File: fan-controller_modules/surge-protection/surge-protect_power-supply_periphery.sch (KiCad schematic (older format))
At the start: 23 parts

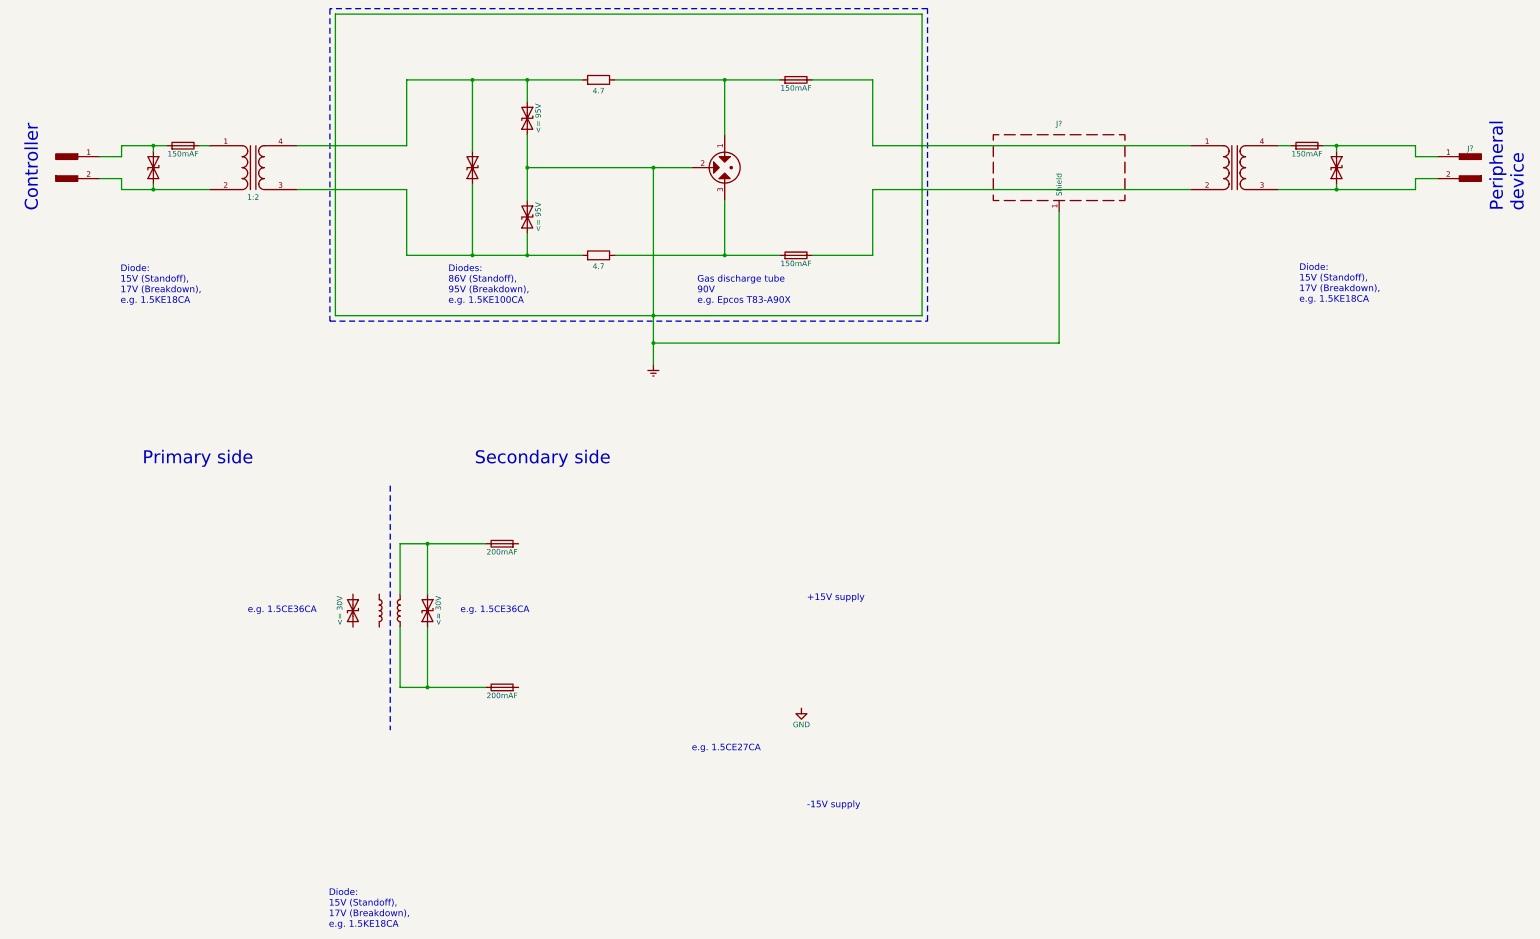
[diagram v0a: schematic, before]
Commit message: Modifying surge protection.
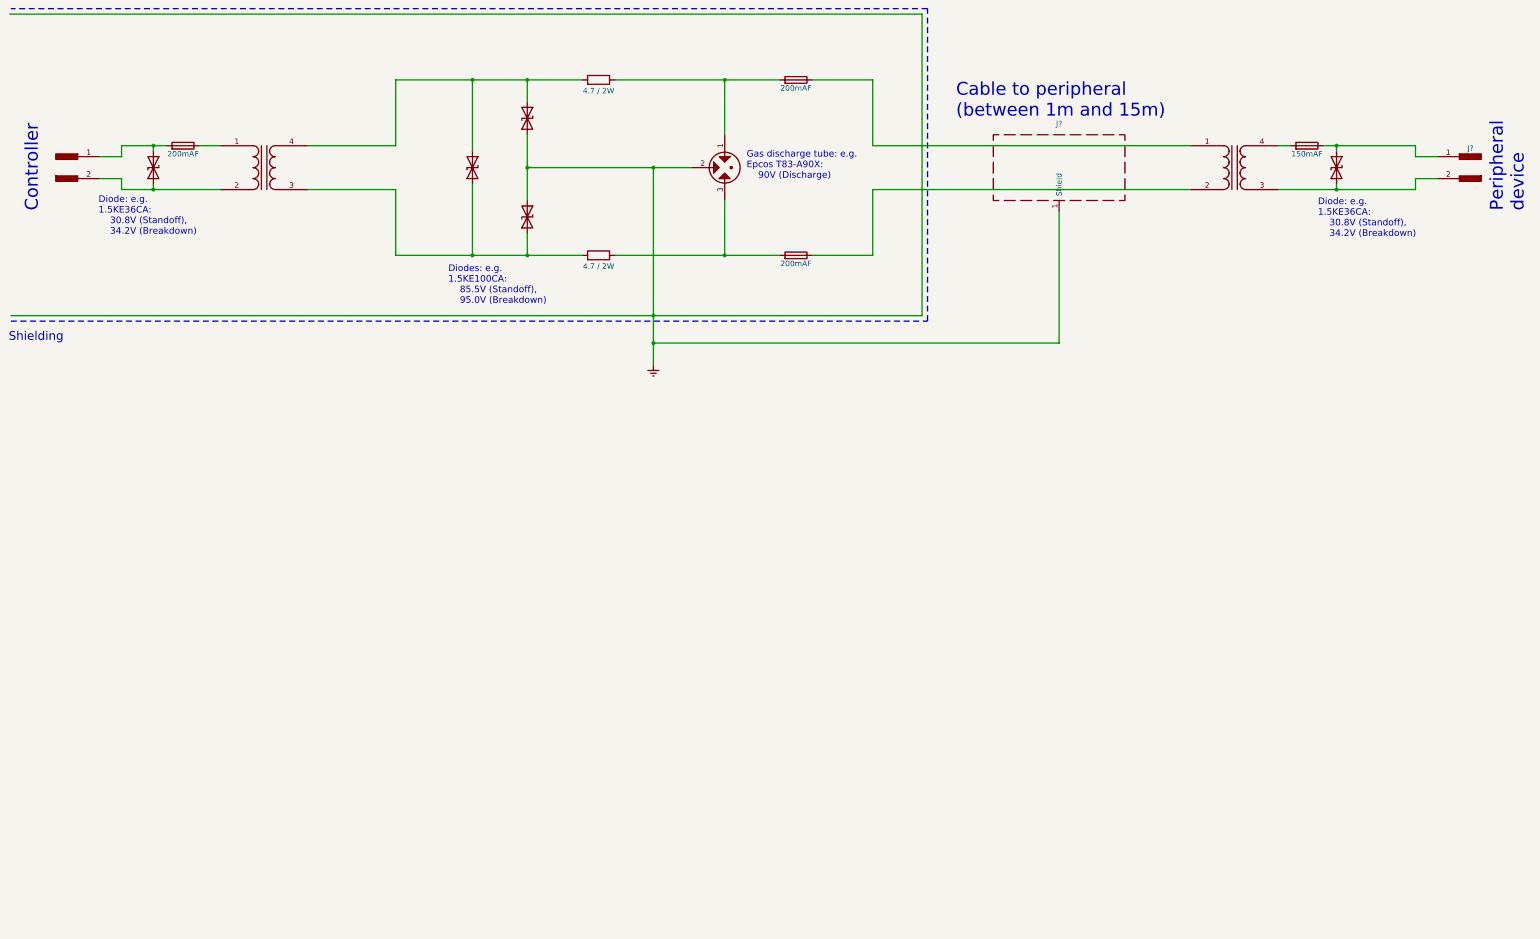
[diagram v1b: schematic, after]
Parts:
- removed D? (x2): <= 30V, symbol D_TVS
- removed F? (x2): 200mAF, symbol Fuse
- removed L? (x2): L, symbol L
- removed T?: 1:2, symbol Transformer_1P_1S
- added T?: 2:1, symbol Transformer_1P_1S
- F? (x3): value 150mAF -> 200mAF
- R? (x2): value 4.7 -> 4.7 / 2W
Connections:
- net labels removed: GND
- wire segments 53 -> 61
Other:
- note added: "Cable to peripheral\n(between 1m and 15m)"
- note added: "Diode: e.g.\n1.5KE36CA:\n 30.8V (Standoff),\n 34.2V (Breakdown)\n"
- note added: "Diodes: e.g.\n1.5KE100CA:\n 85.5V (Standoff),\n 95.0V (Breakdown)"
- note added: "Gas discharge tube: e.g.\nEpcos T83-A90X:\n 90V (Discharge)"
- note added: "Shielding"
- note removed: "+15V supply"
- note removed: "-15V supply"
- note removed: "Diode: \n15V (Standoff),\n17V (Breakdown),\ne.g. 1.5KE18CA"
- note removed: "Diodes: \n86V (Standoff),\n95V (Breakdown),\ne.g. 1.5KE100CA"
- note removed: "Gas discharge tube\n90V\ne.g. Epcos T83-A90X"
- note removed: "Primary side"
- note removed: "Secondary side"
- note removed: "e.g. 1.5CE27CA"
- note removed: "e.g. 1.5CE36CA"
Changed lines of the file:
@@
 encoding utf-8
 Sheet 4 4
-Title ""
+Title "Surge protection, periphery power"
 Date ""
 Rev ""
@@
 $Comp
 L D_TVS D?
-U 1 1 59960DDD
-P 4680 9220
-F 0 "D?" H 4680 9320 50  0001 C CNN
-F 1 "<= 30V" H 4680 9340 50  0000 C CNN
-F 2 "" H 4680 9220 50  0001 C CNN
-F 3 "" H 4680 9220 50  0001 C CNN
-	1    4680 9220
-	0    -1   1    0
-$EndComp
-$Comp
-L D_TVS D?
-U 1 1 59960DE3
-P 5360 9220
-F 0 "D?" H 5360 9320 50  0001 C CNN
-F 1 "<= 30V" H 5360 9120 50  0000 C CNN
-F 2 "" H 5360 9220 50  0001 C CNN
-F 3 "" H 5360 9220 50  0001 C CNN
-	1    5360 9220
-	0    -1   1    0
-$EndComp
-$Comp
-L Fuse F?
-U 1 1 59960DE9
-P 6040 8610
-F 0 "F?" V 6120 8610 50  0001 C CNN
-F 1 "200mAF" V 5965 8610 50  0000 C CNN
-F 2 "" V 5970 8610 50  0001 C CNN
-F 3 "" H 6040 8610 50  0001 C CNN
-	1    6040 8610
-	0    -1   -1   0
-$EndComp
-$Comp
-L Fuse F?
-U 1 1 59960DEF
-P 6040 9920
-F 0 "F?" V 6120 9920 50  0001 C CNN
-F 1 "200mAF" V 5965 9920 50  0000 C CNN
-F 2 "" V 5970 9920 50  0001 C CNN
-F 3 "" H 6040 9920 50  0001 C CNN
-	1    6040 9920
-	0    -1   -1   0
-$EndComp
-$Comp
-L GND #PWR?
-U 1 1 59960DF5
-P 8770 10110
-F 0 "#PWR?" H 8770 9860 50  0001 C CNN
-F 1 "GND" H 8770 9960 50  0000 C CNN
-F 2 "" H 8770 10110 50  0001 C CNN
-F 3 "" H 8770 10110 50  0001 C CNN
-	1    8770 10110
-	1    0    0    -1
-$EndComp
-Text Notes 3720 9250 0    59   ~ 0
-e.g. 1.5CE36CA
-Text Notes 7770 10510 0    59   ~ 0
-e.g. 1.5CE27CA
-Text Notes 8820 9140 0    60   ~ 0
-+15V supply
-Text Notes 8820 11030 0    60   ~ 0
--15V supply
-Text Notes 2760 7900 0    118  ~ 0
-Primary side
-Text Notes 5790 7900 0    118  ~ 0
-Secondary side
-$Comp
-L L L?
-U 1 1 59960E01
-P 4920 9220
-F 0 "L?" H 4920 9470 50  0001 C CNN
-F 1 "L" H 4920 8970 50  0001 C CNN
-F 2 "" H 4920 9220 50  0001 C CNN
-F 3 "" H 4920 9220 50  0001 C CNN
-	1    4920 9220
-	1    0    0    -1
-$EndComp
-$Comp
-L L L?
-U 1 1 59960E07
-P 5110 9220
-F 0 "L?" H 5110 9470 50  0001 C CNN
-F 1 "L" H 5110 8970 50  0001 C CNN
-F 2 "" H 5110 9220 50  0001 C CNN
-F 3 "" H 5110 9220 50  0001 C CNN
-	1    5110 9220
-	-1   0    0    -1
-$EndComp
-Text Notes 5660 9250 0    59   ~ 0
-e.g. 1.5CE36CA
-Wire Notes Line
-	5020 8080 5020 10310
-Wire Wire Line
-	5890 8610 5110 8610
-Wire Wire Line
-	5110 8610 5110 9070
-Wire Wire Line
-	5890 9920 5110 9920
-Wire Wire Line
-	5110 9920 5110 9370
-Wire Wire Line
-	5360 9370 5360 9920
-Connection ~ 5360 9920
-Wire Wire Line
-	5360 9070 5360 8610
-Connection ~ 5360 8610
-Text Notes 4460 12120 0    60   ~ 0
-Diode: \n15V (Standoff),\n17V (Breakdown),\ne.g. 1.5KE18CA
-$Comp
-L D_TVS D?
 U 1 1 5996122F
 P 6270 4730
 F 0 "D?" H 6270 4830 50  0001 C CNN
-F 1 "<= 95V" H 6270 4630 50  0000 C CNN
+F 1 "<= 95V" H 6270 4630 50  0001 C CNN
 F 2 "" H 6270 4730 50  0001 C CNN
 F 3 "" H 6270 4730 50  0001 C CNN
@@
 P 6270 5630
 F 0 "D?" H 6270 5730 50  0001 C CNN
-F 1 "<= 95V" H 6270 5530 50  0000 C CNN
+F 1 "<= 95V" H 6270 5530 50  0001 C CNN
 F 2 "" H 6270 5630 50  0001 C CNN
 F 3 "" H 6270 5630 50  0001 C CNN
@@
 P 6920 4380
 F 0 "R?" V 7000 4380 50  0001 C CNN
-F 1 "4.7" V 6820 4380 50  0000 C CNN
+F 1 "4.7 / 2W" V 6820 4380 50  0000 C CNN
 F 2 "" V 6850 4380 50  0001 C CNN
 F 3 "" H 6920 4380 50  0001 C CNN
@@
 P 6920 5980
 F 0 "R?" V 7000 5980 50  0001 C CNN
-F 1 "4.7" V 6820 5980 50  0000 C CNN
+F 1 "4.7 / 2W" V 6820 5980 50  0000 C CNN
 F 2 "" V 6850 5980 50  0001 C CNN
 F 3 "" H 6920 5980 50  0001 C CNN
@@
 P 8720 4380
 F 0 "F?" V 8800 4380 50  0001 C CNN
-F 1 "150mAF" V 8645 4380 50  0000 C CNN
+F 1 "200mAF" V 8645 4380 50  0000 C CNN
 F 2 "" V 8650 4380 50  0001 C CNN
 F 3 "" H 8720 4380 50  0001 C CNN
@@
 P 8720 5980
 F 0 "F?" V 8800 5980 50  0001 C CNN
-F 1 "150mAF" V 8645 5980 50  0000 C CNN
+F 1 "200mAF" V 8645 5980 50  0000 C CNN
 F 2 "" V 8650 5980 50  0001 C CNN
 F 3 "" H 8720 5980 50  0001 C CNN
@@
 $EndComp
 Wire Notes Line
-	4470 3730 4470 6580
-Wire Notes Line
 	9920 6580 9920 3730
 Wire Wire Line
-	4520 3780 9870 3780
+	1550 3780 9870 3780
 Wire Wire Line
 	9870 3780 9870 6530
 Wire Wire Line
-	9870 6530 4520 6530
-Wire Wire Line
-	4520 6530 4520 3780
+	9870 6530 7420 6530
+Wire Wire Line
+	7420 6530 1560 6530
 $Comp
 L Earth #PWR?
@@
 $EndComp
 Wire Wire Line
-	7070 4380 8570 4380
-Wire Wire Line
-	7070 5980 8570 5980
+	7070 4380 8070 4380
+Wire Wire Line
+	8070 4380 8570 4380
+Wire Wire Line
+	7070 5980 8070 5980
+Wire Wire Line
+	8070 5980 8570 5980
 Wire Wire Line
 	8070 4880 8070 4380
@@
 Connection ~ 8070 5980
 Wire Wire Line
-	6270 4880 6270 5480
-Wire Wire Line
-	6270 5180 7770 5180
+	6270 4880 6270 5180
+Wire Wire Line
+	6270 5180 6270 5480
+Wire Wire Line
+	6270 5180 7420 5180
+Wire Wire Line
+	7420 5180 7770 5180
 Connection ~ 6270 5180
 Wire Wire Line
 	6270 4380 6270 4580
 Wire Wire Line
-	5170 4380 6770 4380
-Wire Wire Line
 	6270 5980 6270 5780
 Wire Wire Line
-	5170 5980 6770 5980
+	5070 5980 5770 5980
+Wire Wire Line
+	5770 5980 6270 5980
+Wire Wire Line
+	6270 5980 6770 5980
 Wire Wire Line
 	5770 5030 5770 4380
@@
 Connection ~ 6270 5980
 Wire Wire Line
-	7420 5180 7420 6980
+	7420 5180 7420 6530
+Wire Wire Line
+	7420 6530 7420 6780
+Wire Wire Line
+	7420 6780 7420 6980
 Connection ~ 7420 6530
 Connection ~ 7420 5180
-Wire Wire Line
-	5170 4980 5170 4380
-Connection ~ 5770 4380
-Wire Wire Line
-	5170 5380 5170 5980
-Connection ~ 5770 5980
 Wire Wire Line
 	8870 4380 9420 4380
@@
 	1    0    0    -1
 $EndComp
-$Comp
-L Transformer_1P_1S T?
-U 1 1 5996129C
-P 3770 5180
-F 0 "T?" H 3770 5430 50  0001 C CNN
-F 1 "1:2" H 3770 4910 50  0000 C CNN
-F 2 "" H 3770 5180 50  0001 C CNN
-F 3 "" H 3770 5180 50  0001 C CNN
-	1    3770 5180
-	1    0    0    -1
-$EndComp
-Wire Wire Line
-	4170 4980 5170 4980
-Wire Wire Line
-	4170 5380 5170 5380
 Wire Wire Line
 	2370 5080 2570 5080
@@
 	2570 5080 2570 4980
 Wire Wire Line
-	2570 4980 2980 4980
+	2570 4980 2860 4980
+Wire Wire Line
+	2860 4980 2980 4980
 Wire Wire Line
 	2370 5280 2570 5280
@@
 	2570 5280 2570 5380
 Wire Wire Line
-	2570 5380 3370 5380
-Wire Wire Line
-	13120 5380 14370 5380
+	13120 5380 13650 5380
+Wire Wire Line
+	13650 5380 14370 5380
 Wire Wire Line
 	14370 5380 14370 5280
@@
 	2860 4980 2860 5030
 Wire Wire Line
-	2860 5330 2860 5380
-Connection ~ 2860 5380
+	2860 5380 2860 5330
 Wire Notes Line
-	9920 3730 4470 3730
+	9920 3730 1560 3730
 Wire Notes Line
-	4470 6580 9920 6580
+	1560 6580 9920 6580
 Text Notes 5550 6430 0    60   ~ 0
-Diodes: \n86V (Standoff),\n95V (Breakdown),\ne.g. 1.5KE100CA
-Text Notes 7820 6430 0    60   ~ 0
-Gas discharge tube\n90V\ne.g. Epcos T83-A90X
-Text Notes 2560 6430 0    60   ~ 0
-Diode: \n15V (Standoff),\n17V (Breakdown),\ne.g. 1.5KE18CA
+Diodes: e.g.\n1.5KE100CA:\n    85.5V (Standoff),\n    95.0V (Breakdown)
+Text Notes 8270 5290 0    60   ~ 0
+Gas discharge tube: e.g.\nEpcos T83-A90X:\n    90V (Discharge)
+Text Notes 2360 5800 0    60   ~ 0
+Diode: e.g.\n1.5KE36CA:\n    30.8V (Standoff),\n    34.2V (Breakdown)\n
 $Comp
 L Fuse F?
@@
 P 3130 4980
 F 0 "F?" V 3210 4980 50  0001 C CNN
-F 1 "150mAF" V 3055 4980 50  0000 C CNN
+F 1 "200mAF" V 3055 4980 50  0000 C CNN
 F 2 "" V 3060 4980 50  0001 C CNN
 F 3 "" H 3130 4980 50  0001 C CNN
@@
 $EndComp
 Connection ~ 2860 4980
-Wire Wire Line
-	3280 4980 3370 4980
 $Comp
 L Fuse F?
@@
 	13120 4980 13230 4980
 Wire Wire Line
-	13530 4980 14370 4980
+	13530 4980 13650 4980
+Wire Wire Line
+	13650 4980 14370 4980
 Wire Wire Line
 	13650 4980 13650 5030
@@
 	14370 5080 14370 4980
 Connection ~ 13650 4980
-Text Notes 13310 6420 0    60   ~ 0
-Diode: \n15V (Standoff),\n17V (Breakdown),\ne.g. 1.5KE18CA
+Text Notes 13480 5820 0    60   ~ 0
+Diode: e.g.\n1.5KE36CA:\n    30.8V (Standoff),\n    34.2V (Breakdown)\n
+Wire Wire Line
+	5070 4380 5770 4380
+Wire Wire Line
+	5770 4380 6270 4380
+Wire Wire Line
+	6270 4380 6770 4380
+$Comp
+L Transformer_1P_1S T?
+U 1 1 5996974A
+P 3870 5180
+F 0 "T?" H 3870 5430 50  0001 C CNN
+F 1 "2:1" H 3870 4880 50  0001 C CNN
+F 2 "" H 3870 5180 50  0001 C CNN
+F 3 "" H 3870 5180 50  0001 C CNN
+	1    3870 5180
+	1    0    0    -1
+$EndComp
+Wire Wire Line
+	3280 4980 3470 4980
+Wire Wire Line
+	2570 5380 2860 5380
+Wire Wire Line
+	2860 5380 3470 5380
+Connection ~ 2860 5380
+Wire Wire Line
+	4270 4980 5070 4980
+Wire Wire Line
+	5070 4980 5070 4380
+Connection ~ 5770 4380
+Wire Wire Line
+	4270 5380 5070 5380
+Wire Wire Line
+	5070 5380 5070 5980
+Connection ~ 5770 5980
+Text Notes 10180 4730 0    118  ~ 0
+Cable to peripheral\n(between 1m and 15m)
+Text Notes 1540 6770 0    79   ~ 0
+Shielding
 $EndSCHEMATC
